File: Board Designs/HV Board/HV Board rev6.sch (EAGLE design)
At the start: 65 parts, among them IC1 OKI-78SR, IC2 NE5532SOIC

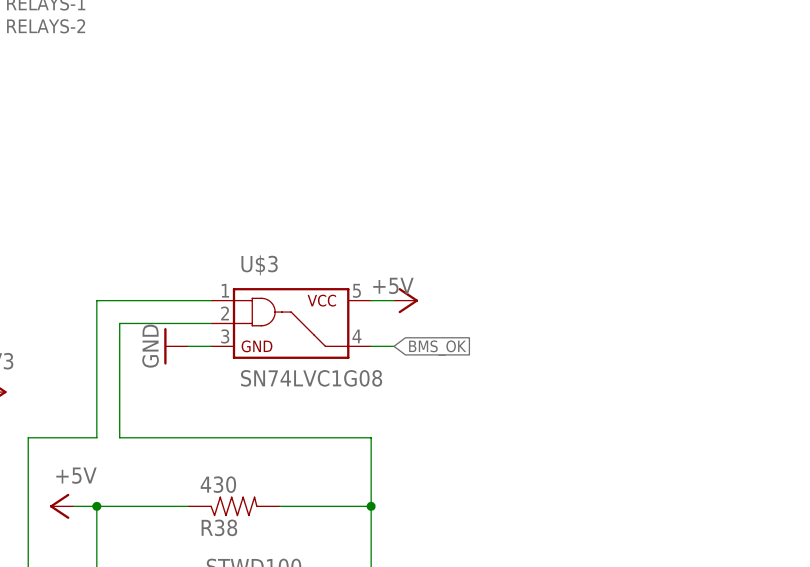
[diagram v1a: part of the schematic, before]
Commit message: Fixed NAND gate input
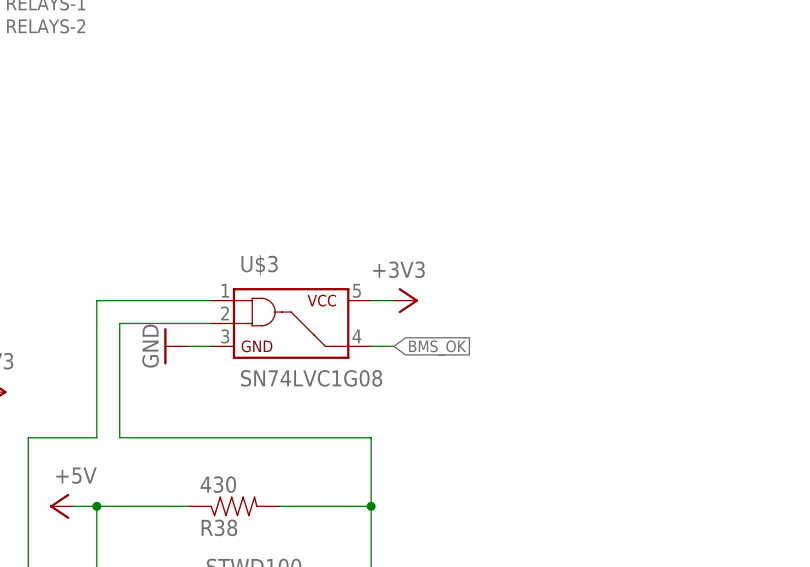
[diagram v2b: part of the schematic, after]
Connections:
- net +3V3: now also U$3.5
- net +5V: no longer U$3.5
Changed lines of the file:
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@@
 <part name="GND17" library="supply1" deviceset="GND" device=""/>
 <part name="U$3" library="HyTechDevices" deviceset="SN74LVC1G08" device=""/>
-<part name="P+9" library="supply1" library_urn="urn:adsk.eagle:library:371" deviceset="+5V" device=""/>
 <part name="HV+UNFUSED" library="HyTechDevices" deviceset="CONNECTOR-2" device="NANO-FIT_VERTICAL-2" value="HV+UNFUSED"/>
 <part name="HV-UNFUSED" library="HyTechDevices" deviceset="CONNECTOR-2" device="NANO-FIT_VERTICAL-2" value="HV-UNFUSED"/>
 <part name="RELAY_JUMP" library="HyTechDevices" deviceset="CONNECTOR-2" device="NANO-FIT_VERTICAL-2" value="RELAY_JUMPER"/>
 <part name="RELAY" library="HyTechDevices" deviceset="CONNECTOR-2" device="NANO-FIT_VERTICAL-2" value="RELAY_JUMPER"/>
+<part name="+3V3" library="supply1" library_urn="urn:adsk.eagle:library:371" deviceset="+3V3" device=""/>
 </parts>
 <sheets>
@@
 <attribute name="VALUE" x="130.175" y="-177.165" size="1.778" layer="96"/>
 </instance>
-<instance part="P+9" gate="1" x="149.86" y="-167.64" smashed="yes" rot="MR90">
-<attribute name="VALUE" x="144.78" y="-165.1" size="1.778" layer="96" rot="MR180"/>
-</instance>
 <instance part="HV+UNFUSED" gate="-2" x="200.66" y="-83.82" smashed="yes" rot="R180">
 <attribute name="NAME" x="198.12" y="-83.058" size="1.524" layer="95" rot="R180"/>
@@
 <attribute name="NAME" x="71.12" y="19.558" size="1.524" layer="95"/>
 <attribute name="VALUE" x="67.818" y="21.717" size="1.778" layer="96"/>
+</instance>
+<instance part="+3V3" gate="G$1" x="149.86" y="-167.64" smashed="yes" rot="R270">
+<attribute name="VALUE" x="144.78" y="-165.1" size="1.778" layer="96"/>
 </instance>
 </instances>
@@
 <wire x1="86.36" y1="-66.04" x2="83.82" y2="-66.04" width="0.1524" layer="91"/>
 </segment>
-<segment>
-<pinref part="U$3" gate="G$1" pin="5"/>
-<pinref part="P+9" gate="1" pin="+5V"/>
-<wire x1="144.78" y1="-167.64" x2="147.32" y2="-167.64" width="0.1524" layer="91"/>
-</segment>
 </net>
 <net name="TRIM" class="0">
@@
 <wire x1="101.6" y1="-177.8" x2="91.44" y2="-177.8" width="0.1524" layer="91"/>
 </segment>
-</net>
+<segment>
+<pinref part="U$3" gate="G$1" pin="5"/>
+<wire x1="144.78" y1="-167.64" x2="147.32" y2="-167.64" width="0.1524" layer="91"/>
+<pinref part="+3V3" gate="G$1" pin="+3V3"/>
+</segment>
+</net>

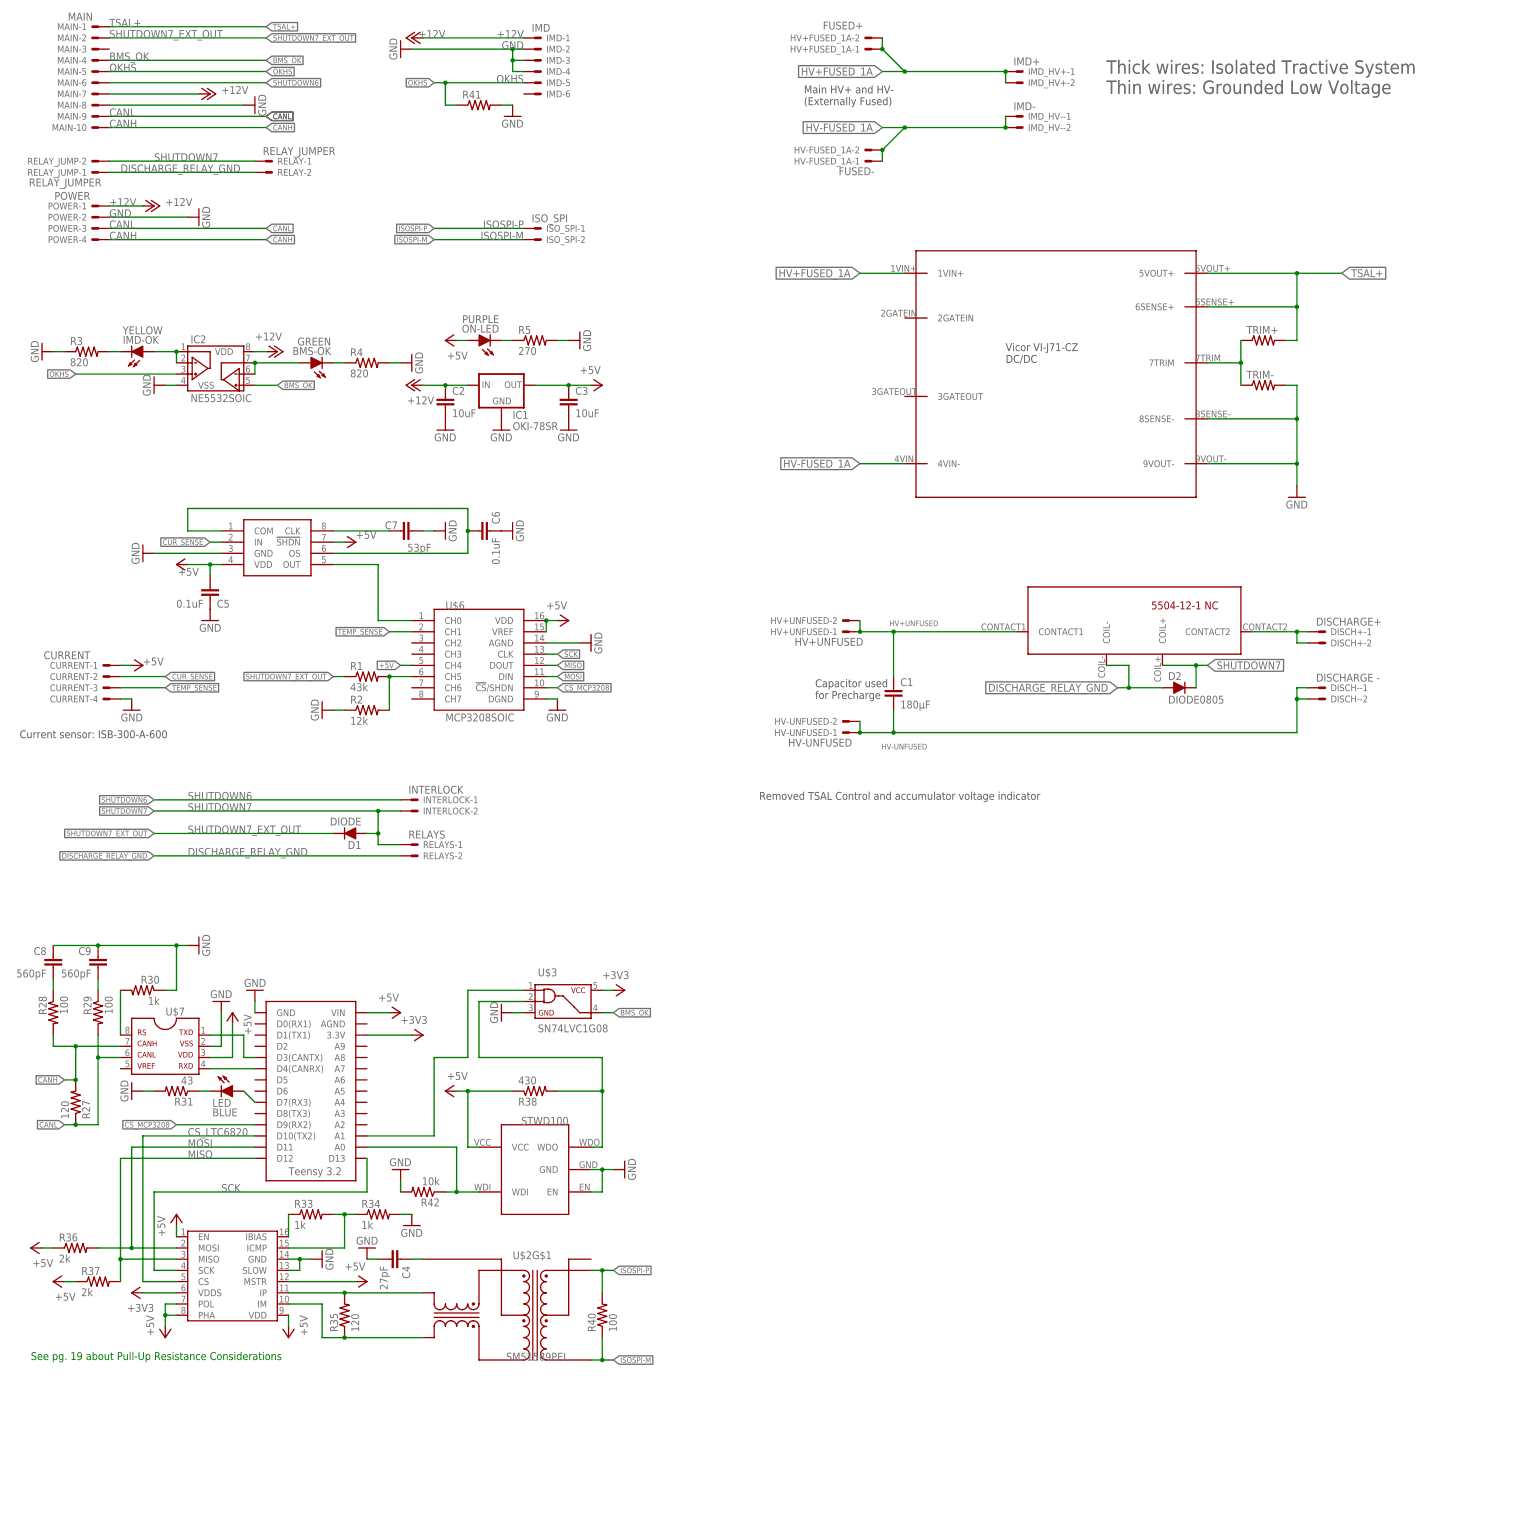
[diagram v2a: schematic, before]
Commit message: Fixed 6820 distance for rev6
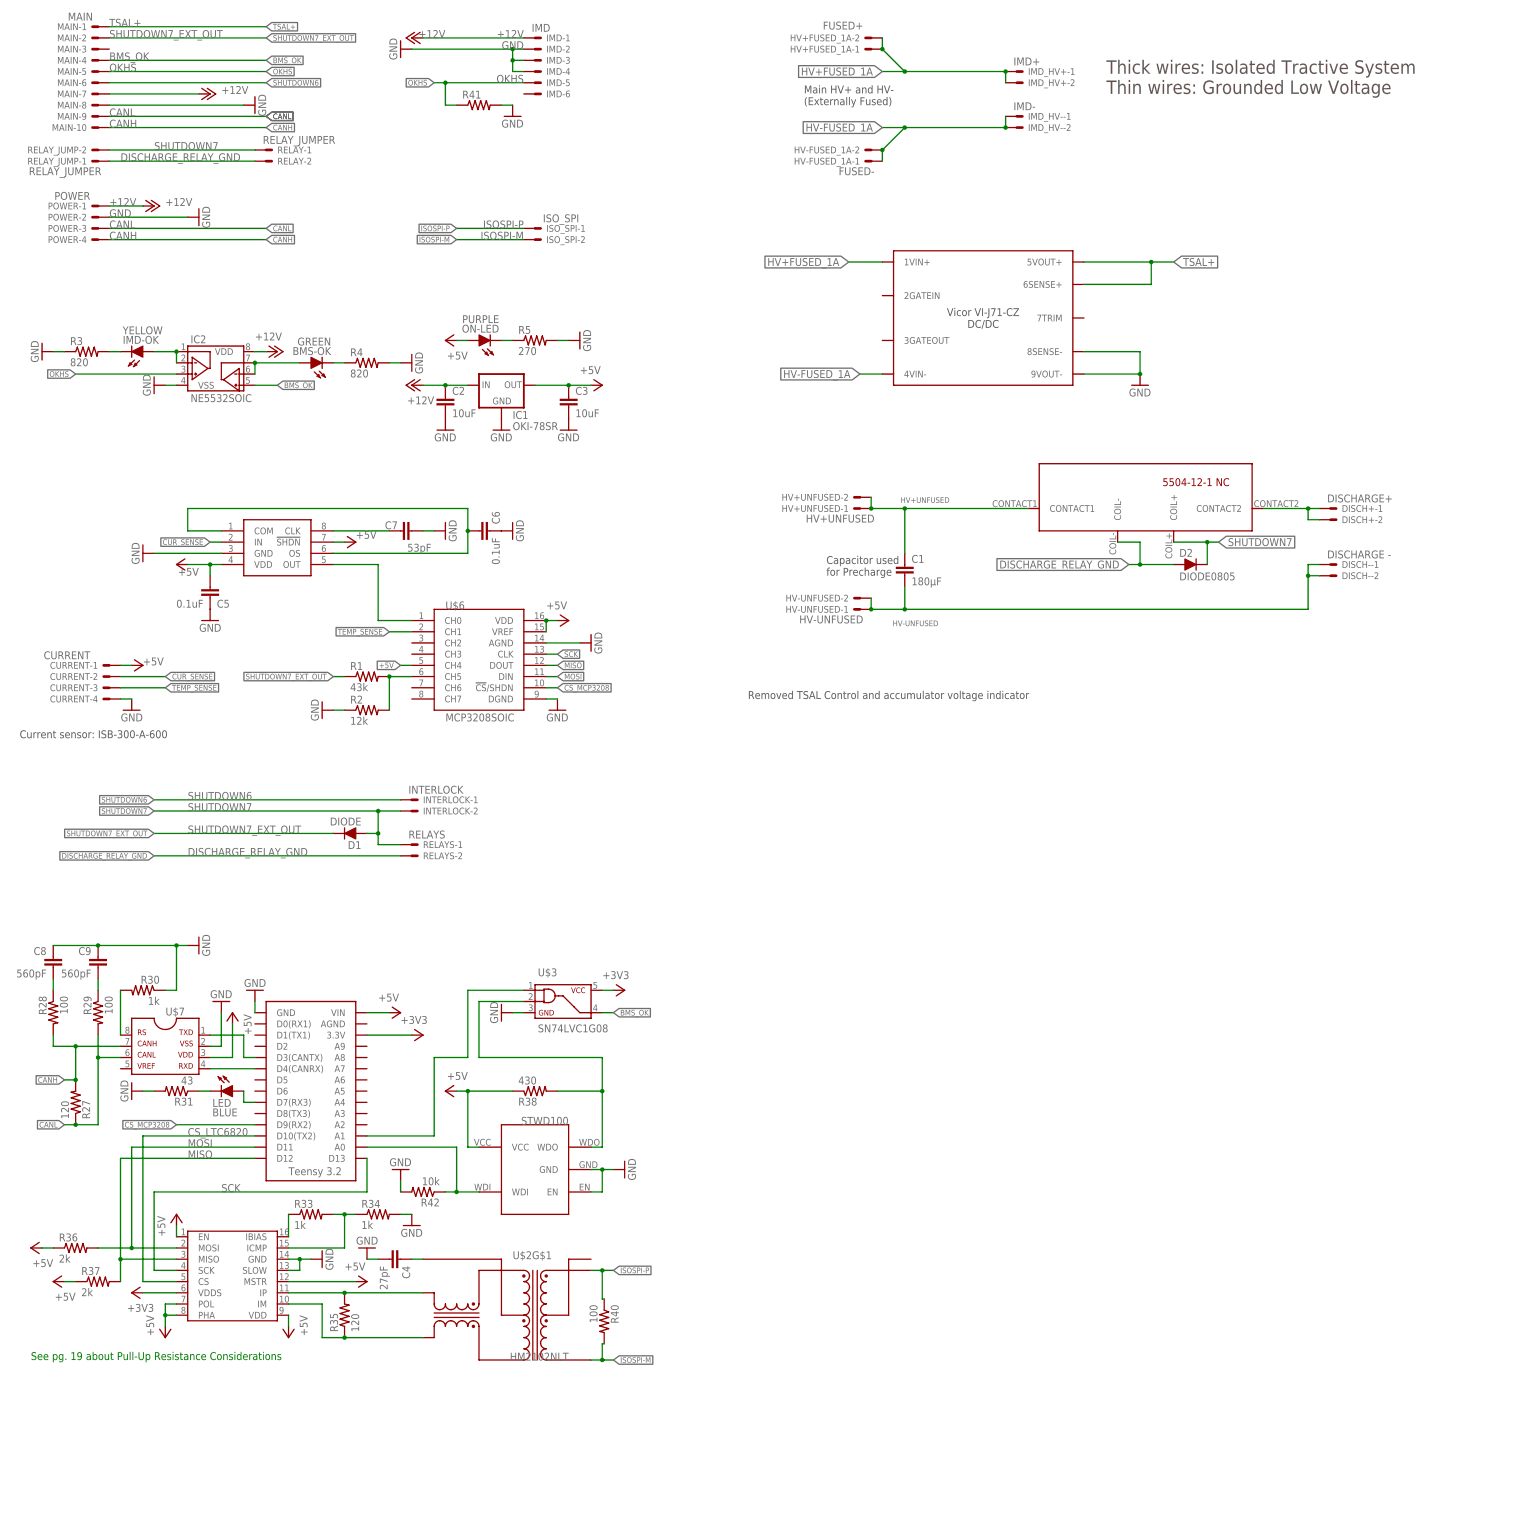
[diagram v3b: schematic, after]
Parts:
- removed TRIM+, TRIM-: (no value), HyTechDevices:RESISTOR0805-RES
- U$2: value SM51589PEL -> HM2102NLT; device HyTechDevices:SM51589PEL -> HyTechDevices:HM2102NLT
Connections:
- removed net TRIM: TRIM+.1, TRIM-.1, U$5.7TRIM
- net GND: no longer TRIM-.2
- net ISOSPI-M: now also R40.2; no longer R40.1
- net ISOSPI-P: now also R40.1; no longer R40.2
- net TSAL+: no longer TRIM+.2
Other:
- moved on the sheet: C1, D2, DISCH+-1, DISCH+-2, DISCH--1, DISCH--2, HV+UNFUSED-1, HV+UNFUSED-2, HV-UNFUSED-1, HV-UNFUSED-2, R40, RELAY-1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

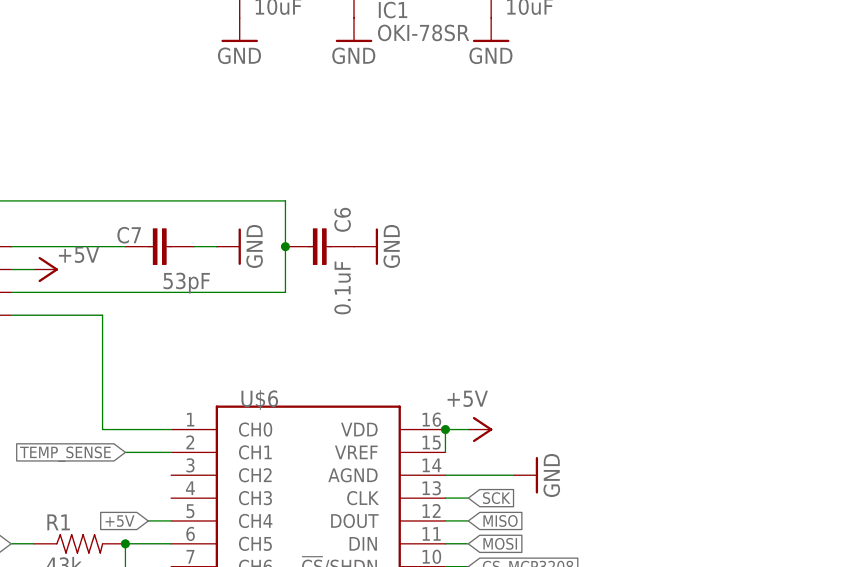
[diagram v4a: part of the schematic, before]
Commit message: HV rev6 & 7: Fixed capacitor value for ADC filter
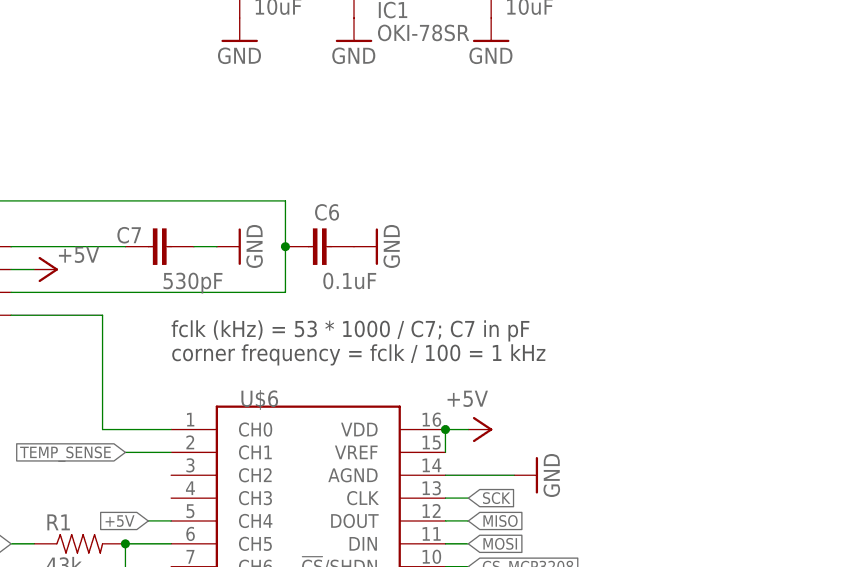
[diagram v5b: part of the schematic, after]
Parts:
- C7: value 53pF -> 530pF
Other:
- note added: "fclk (kHz) = 53 * 1000 / C7; C7 in pF corner frequency = fclk / 100 = 1 kHz"
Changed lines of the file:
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@@
 <layer number="154" name="FabDoc2" color="7" fill="1" visible="yes" active="yes"/>
 <layer number="155" name="FabDoc3" color="7" fill="1" visible="yes" active="yes"/>
+<layer number="156" name="HVSpacing" color="12" fill="1" visible="yes" active="yes"/>
 <layer number="191" name="mNets" color="7" fill="1" visible="yes" active="yes"/>
 <layer number="192" name="mBusses" color="7" fill="1" visible="yes" active="yes"/>
@@
 <part name="C6" library="HyTechDevices" deviceset="CAP" device="0805" value="0.1uF"/>
 <part name="GND10" library="supply1" deviceset="GND" device=""/>
-<part name="C7" library="HyTechDevices" deviceset="CAP" device="0805" value="53pF"/>
+<part name="C7" library="HyTechDevices" deviceset="CAP" device="0805" value="530pF"/>
 <part name="GND14" library="supply1" deviceset="GND" device=""/>
 <part name="MAIN" library="HyTechDevices" deviceset="CONNECTOR-10" device="NANO-FIT_VERTICAL-10" value="MAIN"/>
@@
 <text x="195.58" y="-73.66" size="1.778" layer="97">Capacitor used
 for Precharge</text>
+<text x="101.6" y="-76.2" size="1.778" layer="97">fclk (kHz) = 53 * 1000 / C7; C7 in pF
+corner frequency = fclk / 100 = 1 kHz</text>
 </plain>
 <instances>
@@
 </instance>
 <instance part="C6" gate="G$1" x="119.38" y="-63.5" smashed="yes" rot="MR270">
-<attribute name="NAME" x="119.761" y="-61.976" size="1.778" layer="95" rot="MR90"/>
-<attribute name="VALUE" x="121.539" y="-65.024" size="1.778" layer="96" rot="MR270"/>
+<attribute name="NAME" x="120.396" y="-58.801" size="1.778" layer="95" rot="R180"/>
+<attribute name="VALUE" x="118.364" y="-66.421" size="1.778" layer="96" rot="MR180"/>
 </instance>
 <instance part="GND10" gate="1" x="124.46" y="-63.5" smashed="yes" rot="MR270">
